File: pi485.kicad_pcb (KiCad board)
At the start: 2 copper layers, 48 x 70 mm, 28 parts, among them J1 RS485, P1 Rasperry Pi, P2 PWR, P3 Term, Q1 2N4401, Q2 2N4401, U1 NE555, U2 MAX485

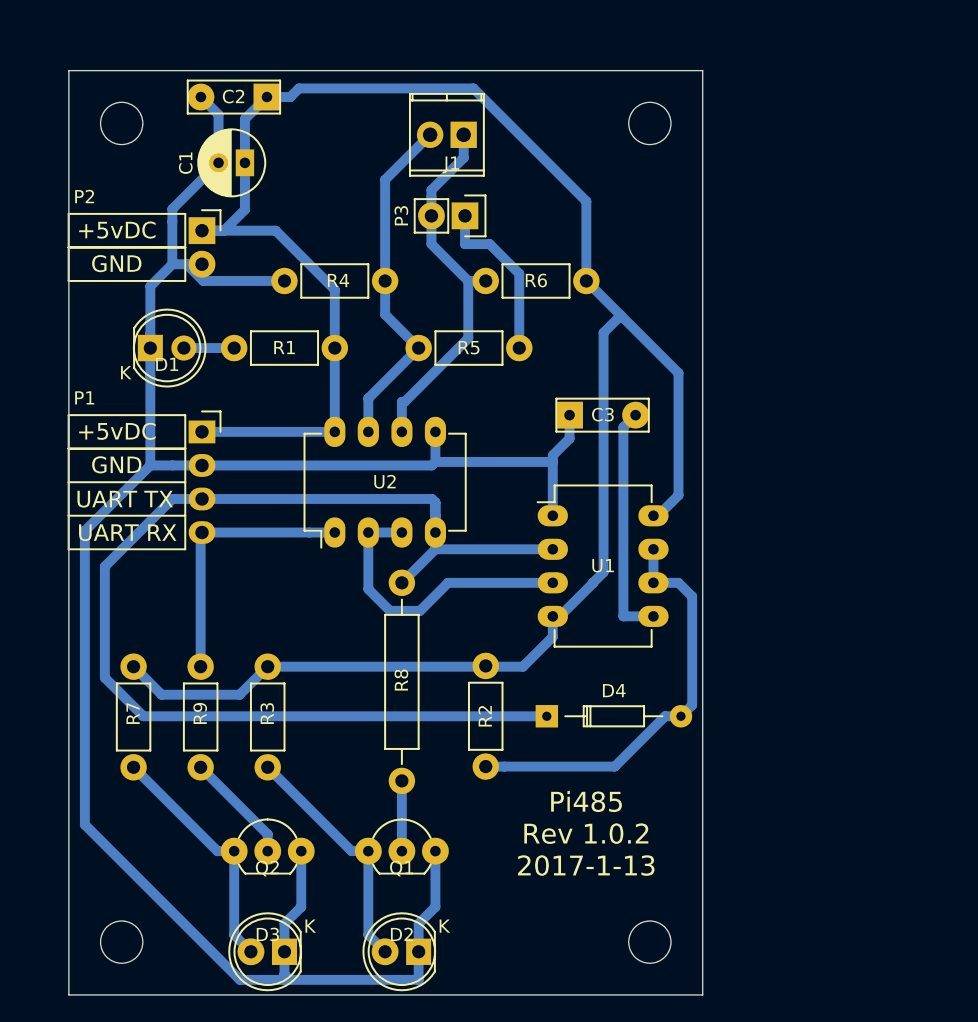
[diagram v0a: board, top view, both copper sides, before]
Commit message: * Rotated board 90 degrees. * Major update to footprints. Resistors are 10mm, LEDs are 3mm. * Manually re-routed / cleaned up traces & positiiong of quite a few things. * This could be pulled so much tighter, but to keep it 'simple soldering' I'm deliberately keeping big honkin traces with lots of clearance. * Fixed a major issue where I had accidentally forgotten the discharge capacitor by deleting the wrong one. The CTRL pin of the 555 should be jumperable to GND to keep the output of the 555 low, regardless of input (latch disable).
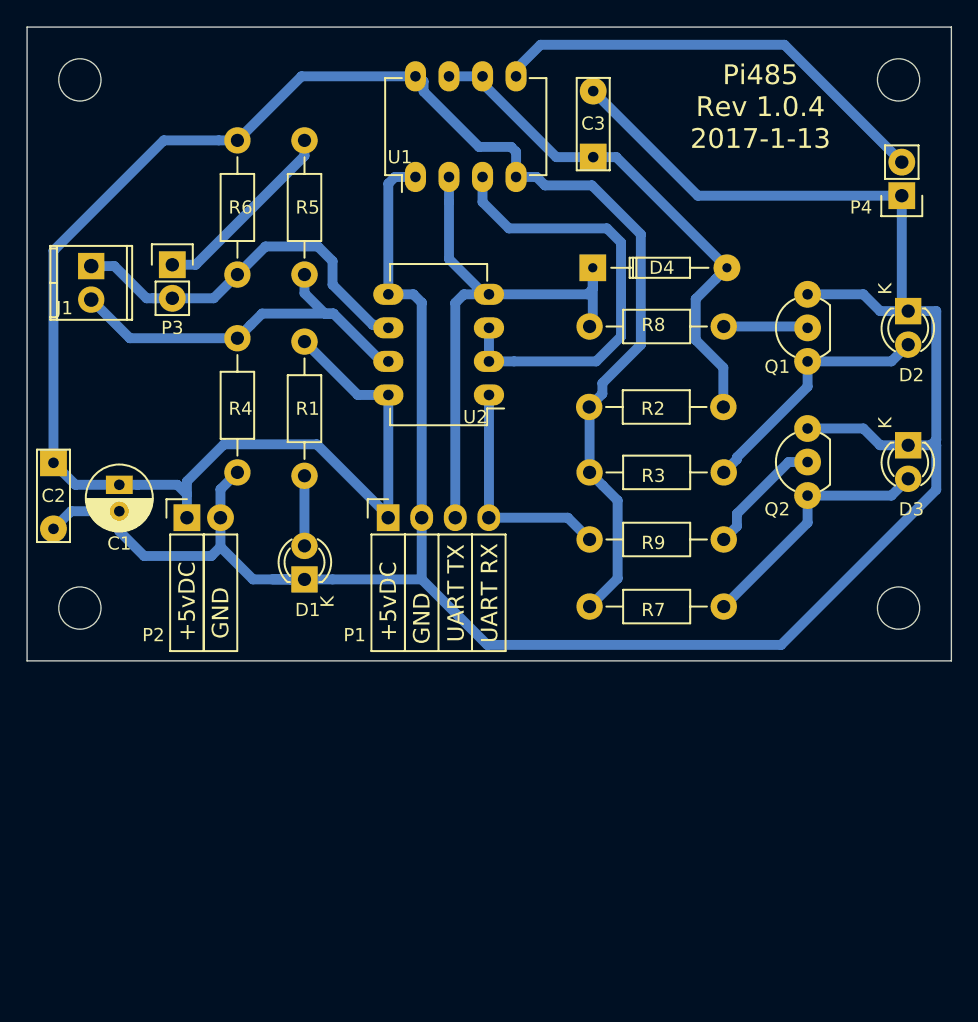
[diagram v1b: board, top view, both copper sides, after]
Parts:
- added P4: Latch Disable, Pin_Headers:Pin_Header_Straight_1x02, F.Cu at (78.6, 25.1)
- D1, D2, D3: footprint LEDs:LED-5MM -> LEDs:LED-3MM
- R1, R2, R3, R4, R5, R6, R7, R9: footprint Resistors_THT:Resistor_Horizontal_RM7mm -> Resistors_THT:Resistor_Horizontal_RM10mm
- R8: footprint Resistors_THT:Resistor_Horizontal_RM15mm -> Resistors_THT:Resistor_Horizontal_RM10mm
- moved REF03 68.0 mm to (78.3, 16.3), turned to 90 degrees
- moved REF04 64.0 mm to (78.3, 56.3), turned to 90 degrees
- moved D2 61.1 mm to (79.1, 33.8), turned to 270 degrees
- moved D3 60.8 mm to (79.1, 44.0), turned to 270 degrees
- moved Q2 51.1 mm to (71.4, 47.8), turned to 90 degrees
- moved Q1 49.8 mm to (71.4, 37.6), turned to 90 degrees
- moved R7 46.3 mm to (65.1, 56.2), turned to 180 degrees
- moved REF02 43.3 mm to (16.3, 16.3), turned to 90 degrees
- moved R9 43.2 mm to (65.1, 51.1), turned to 180 degrees
- moved R8 42.2 mm to (65.1, 35.0), turned to 180 degrees
- moved R3 41.1 mm to (65.1, 46.0), turned to 180 degrees
- moved REF01 36.8 mm to (16.3, 56.3), turned to 90 degrees
- moved D4 34.1 mm to (55.2, 30.5)
- moved R2 32.6 mm to (65.1, 41.1), turned to 180 degrees
- moved C2 32.1 mm to (14.3, 45.3), turned to 270 degrees
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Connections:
- C3 pad 1: GND -> Net-(C3-Pad1)
- C3 pad 2: Net-(C3-Pad2) -> GND
- D4 pad 2: Net-(D4-Pad2) -> Net-(C3-Pad1)
- R2 pad 1: Net-(D4-Pad2) -> Net-(C3-Pad1)
- U1 pad 5: Net-(C3-Pad2) -> Net-(P4-Pad2)
- U1 pad 6: Net-(D4-Pad2) -> Net-(C3-Pad1)
- U1 pad 7: Net-(D4-Pad2) -> Net-(C3-Pad1)
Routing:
- net /(TXDO)_GPIO14: track 88.7 -> 43.9 mm
- net Net-(C3-Pad1): track 0.00 -> 39.7 mm
- net Net-(P4-Pad2): track 0.00 -> 34.2 mm
- net Net-(D4-Pad2): track 31.1 -> 0.00 mm
- net GND: track 161.8 -> 192.4 mm
- net Net-(C3-Pad2): track 17.9 -> 0.00 mm
- net Net-(U1-Pad3): track 22.4 -> 35.2 mm
- net VCC: track 163.2 -> 154.5 mm
- net Net-(J1-Pad2): track 26.5 -> 30.2 mm
- net /(RXDO)_GPIO15: track 20.3 -> 17.6 mm
- net Net-(P3-Pad1): track 12.8 -> 14.6 mm
- net Net-(D1-Pad2): track 3.81 -> 5.56 mm
- net Net-(Q2-Pad2): track 8.45 -> 9.97 mm
- net Net-(Q1-Pad2): track 5.32 -> 6.39 mm
- net Net-(D2-Pad2): track 18.4 -> 19.2 mm
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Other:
- board size 48 x 70 mm -> 70 x 48 mm
- board text added: "Pi485 Rev 1.0.4 2017-1-13"
- board text removed: "Pi485 Rev 1.0.2 2017-1-13"

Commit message: Oh yeah, the date.
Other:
- board text added: "Pi485 Rev 1.0.4 2017-1-16"
- board text removed: "Pi485 Rev 1.0.4 2017-1-13"
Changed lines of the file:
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@@
     (effects (font (size 1.25 1.25) (thickness 0.2)))
   )
-  (gr_text "Pi485\nRev 1.0.4\n2017-1-13" (at 67.871 18.36) (layer F.SilkS)
+  (gr_text "Pi485\nRev 1.0.4\n2017-1-16" (at 67.871 18.36) (layer F.SilkS)
     (effects (font (size 1.5 1.5) (thickness 0.3)))
   )

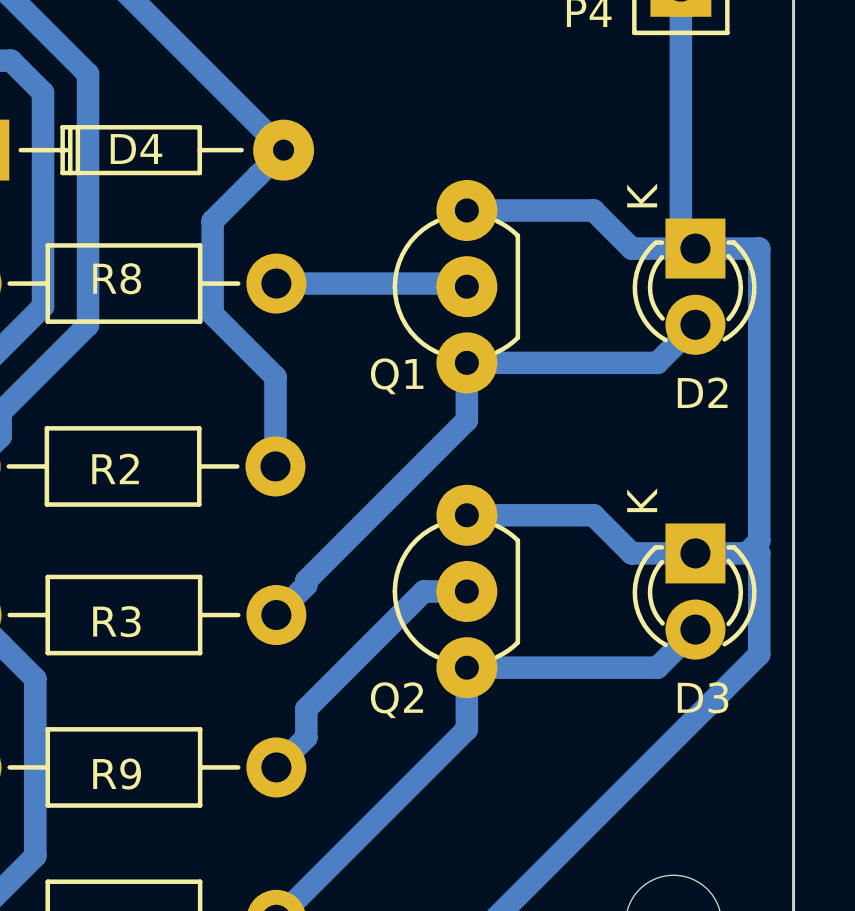
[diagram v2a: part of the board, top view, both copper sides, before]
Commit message: Fixed the footprint issues with the 2N4401 transistors being 'backwards'
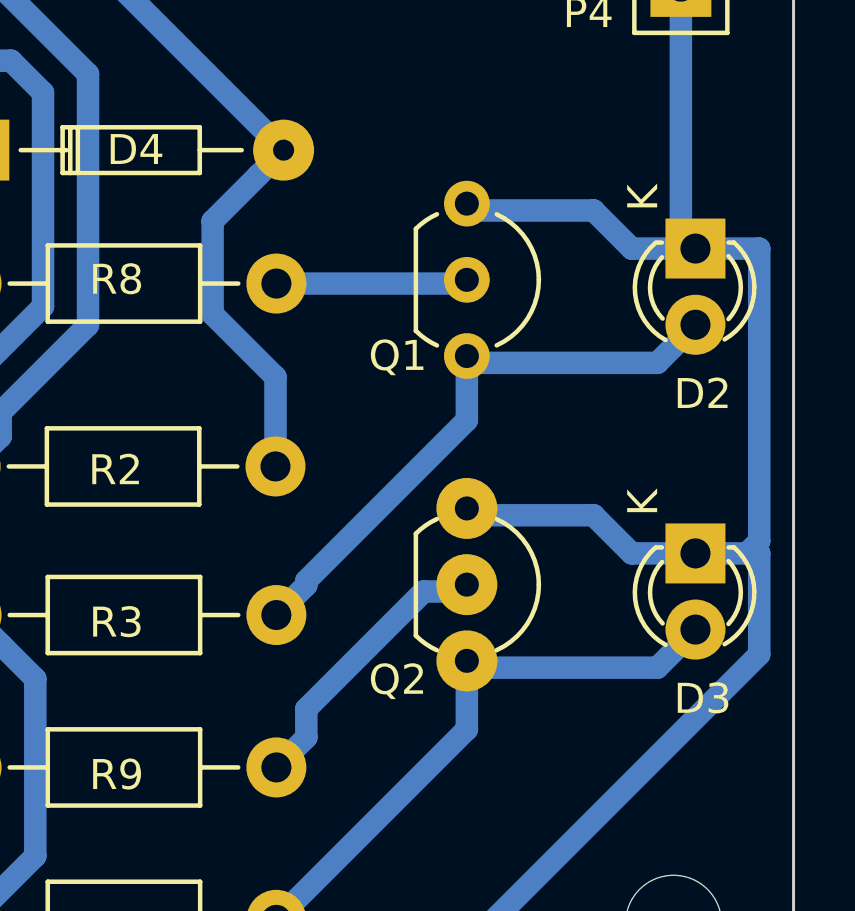
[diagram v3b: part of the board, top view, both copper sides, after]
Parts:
- moved Q1 5.31 mm to (71.4, 32.3), turned to 270 degrees
- moved Q2 5.31 mm to (71.4, 42.5), turned to 270 degrees
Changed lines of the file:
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@@
   (general
     (links 51)
-    (no_connects 0)
+    (no_connects 1)
     (area 10.622919 6.135856 84.172919 66.500142)
     (thickness 1.6)
@@
     (add_net VCC)
   )
+  (module TO_SOT_Packages_THT:TO-92_Inline_Wide placed (layer F.Cu)
+    (at 71.440419 42.49 270)
+    (descr "TO-92 leads in-line, wide, drill 0.8mm (see NXP sot054_po.pdf)")
+    (tags "to-92 sc-43 sc-43a sot54 PA33 transistor")
+    (fp_text reference Q2 (at 5.715 2.299419 360) (layer F.SilkS)
+      (effects (font (size 1 1) (thickness 0.15)))
+    )
+    (fp_text value 2N4401 (at -1.905 0.394419 360) (layer F.Fab)
+      (effects (font (size 1 1) (thickness 0.15)))
+    )
+    (fp_line (start 6.1 1.95) (end 6.1 -2.65) (layer F.CrtYd) (width 0.05))
+    (fp_line (start -1 -2.65) (end 6.1 -2.65) (layer F.CrtYd) (width 0.05))
+    (fp_arc (start 2.54 0) (end 2.54 -2.4) (angle 65.55604127) (layer F.SilkS) (width 0.15))
+    (fp_arc (start 2.54 0) (end 2.54 -2.4) (angle -65.55604127) (layer F.SilkS) (width 0.15))
+    (fp_line (start 0.84 1.7) (end 4.24 1.7) (layer F.SilkS) (width 0.15))
+    (fp_line (start -1 1.95) (end 6.1 1.95) (layer F.CrtYd) (width 0.05))
+    (fp_line (start -1 1.95) (end -1 -2.65) (layer F.CrtYd) (width 0.05))
+    (fp_arc (start 2.54 0) (end 4.24 1.7) (angle -20.5) (layer F.SilkS) (width 0.15))
+    (fp_arc (start 2.54 0) (end 0.84 1.7) (angle 20.5) (layer F.SilkS) (width 0.15))
+    (pad 1 thru_hole circle (at 5.08 0) (size 2.032 2.032) (drill 0.8) (layers *.Cu *.Mask)
+      (net 4 "Net-(D3-Pad2)"))
+    (pad 3 thru_hole circle (at 0 0) (size 2.032 2.032) (drill 0.8) (layers *.Cu *.Mask)
+      (net 2 GND))
+    (pad 2 thru_hole circle (at 2.54 0) (size 2.032 2.032) (drill 0.8) (layers *.Cu *.Mask)
+      (net 5 "Net-(Q2-Pad2)"))
+    (model TO_SOT_Packages_THT.3dshapes/TO-92_Inline_Wide.wrl
+      (at (xyz 0.1 0 0))
+      (scale (xyz 1 1 1))
+      (rotate (xyz 0 0 -90))
+    )
+  )
+  (module TO_SOT_Packages_THT:TO-92_Inline_Wide (layer F.Cu)
+    (at 71.440419 32.33 270)
+    (descr "TO-92 leads in-line, wide, drill 0.8mm (see NXP sot054_po.pdf)")
+    (tags "to-92 sc-43 sc-43a sot54 PA33 transistor")
+    (fp_text reference Q1 (at 5.08 2.299419 540) (layer F.SilkS)
+      (effects (font (size 1 1) (thickness 0.15)))
+    )
+    (fp_text value 2N4401 (at -1.905 0.394419 360) (layer F.Fab)
+      (effects (font (size 1 1) (thickness 0.15)))
+    )
+    (fp_line (start 6.1 1.95) (end 6.1 -2.65) (layer F.CrtYd) (width 0.05))
+    (fp_line (start -1 -2.65) (end 6.1 -2.65) (layer F.CrtYd) (width 0.05))
+    (fp_arc (start 2.54 0) (end 2.54 -2.4) (angle 65.55604127) (layer F.SilkS) (width 0.15))
+    (fp_arc (start 2.54 0) (end 2.54 -2.4) (angle -65.55604127) (layer F.SilkS) (width 0.15))
+    (fp_line (start 0.84 1.7) (end 4.24 1.7) (layer F.SilkS) (width 0.15))
+    (fp_line (start -1 1.95) (end 6.1 1.95) (layer F.CrtYd) (width 0.05))
+    (fp_line (start -1 1.95) (end -1 -2.65) (layer F.CrtYd) (width 0.05))
+    (fp_arc (start 2.54 0) (end 4.24 1.7) (angle -20.5) (layer F.SilkS) (width 0.15))
+    (fp_arc (start 2.54 0) (end 0.84 1.7) (angle 20.5) (layer F.SilkS) (width 0.15))
+    (pad 1 thru_hole circle (at 5.08 0) (size 1.524 1.524) (drill 0.8) (layers *.Cu *.Mask)
+      (net 3 "Net-(D2-Pad2)"))
+    (pad 3 thru_hole circle (at 0 0) (size 1.524 1.524) (drill 0.8) (layers *.Cu *.Mask)
+      (net 2 GND))
+    (pad 2 thru_hole circle (at 2.54 0) (size 1.524 1.524) (drill 0.8) (layers *.Cu *.Mask)
+      (net 1 "Net-(Q1-Pad2)"))
+    (model TO_SOT_Packages_THT.3dshapes/TO-92_Inline_Wide.wrl
+      (at (xyz 0.1 0 0))
+      (scale (xyz 1 1 1))
+      (rotate (xyz 0 0 -90))
+    )
+  )
   (module Resistors_THT:Resistor_Horizontal_RM10mm (layer F.Cu)
     (at 65.090419 34.994199 180)
@@
     )
   )
-  (module TO_SOT_Packages_THT:TO-92_Inline_Wide placed (layer F.Cu)
-    (at 71.440419 47.797999 90)
-    (descr "TO-92 leads in-line, wide, drill 0.8mm (see NXP sot054_po.pdf)")
-    (tags "to-92 sc-43 sc-43a sot54 PA33 transistor")
-    (fp_text reference Q2 (at -1.042001 -2.299419 180) (layer F.SilkS)
-      (effects (font (size 1 1) (thickness 0.15)))
-    )
-    (fp_text value 2N4401 (at 7.212999 -0.394419 180) (layer F.Fab)
-      (effects (font (size 1 1) (thickness 0.15)))
-    )
-    (fp_line (start 6.1 1.95) (end 6.1 -2.65) (layer F.CrtYd) (width 0.05))
-    (fp_line (start -1 -2.65) (end 6.1 -2.65) (layer F.CrtYd) (width 0.05))
-    (fp_arc (start 2.54 0) (end 2.54 -2.4) (angle 65.55604127) (layer F.SilkS) (width 0.15))
-    (fp_arc (start 2.54 0) (end 2.54 -2.4) (angle -65.55604127) (layer F.SilkS) (width 0.15))
-    (fp_line (start 0.84 1.7) (end 4.24 1.7) (layer F.SilkS) (width 0.15))
-    (fp_line (start -1 1.95) (end 6.1 1.95) (layer F.CrtYd) (width 0.05))
-    (fp_line (start -1 1.95) (end -1 -2.65) (layer F.CrtYd) (width 0.05))
-    (fp_arc (start 2.54 0) (end 4.24 1.7) (angle -20.5) (layer F.SilkS) (width 0.15))
-    (fp_arc (start 2.54 0) (end 0.84 1.7) (angle 20.5) (layer F.SilkS) (width 0.15))
-    (pad 1 thru_hole circle (at 0 0 180) (size 2.032 2.032) (drill 0.8) (layers *.Cu *.Mask)
-      (net 4 "Net-(D3-Pad2)"))
-    (pad 3 thru_hole circle (at 5.08 0 180) (size 2.032 2.032) (drill 0.8) (layers *.Cu *.Mask)
-      (net 2 GND))
-    (pad 2 thru_hole circle (at 2.54 0 180) (size 2.032 2.032) (drill 0.8) (layers *.Cu *.Mask)
-      (net 5 "Net-(Q2-Pad2)"))
-    (model TO_SOT_Packages_THT.3dshapes/TO-92_Inline_Wide.wrl
-      (at (xyz 0.1 0 0))
-      (scale (xyz 1 1 1))
-      (rotate (xyz 0 0 -90))
-    )
-  )
-  (module TO_SOT_Packages_THT:TO-92_Inline_Wide placed (layer F.Cu)
-    (at 71.440419 37.637999 90)
-    (descr "TO-92 leads in-line, wide, drill 0.8mm (see NXP sot054_po.pdf)")
-    (tags "to-92 sc-43 sc-43a sot54 PA33 transistor")
-    (fp_text reference Q1 (at -0.407001 -2.299419) (layer F.SilkS)
-      (effects (font (size 1 1) (thickness 0.15)))
-    )
-    (fp_text value 2N4401 (at 7.212999 -0.394419 180) (layer F.Fab)
-      (effects (font (size 1 1) (thickness 0.15)))
-    )
-    (fp_arc (start 2.54 0) (end 0.84 1.7) (angle 20.5) (layer F.SilkS) (width 0.15))
-    (fp_arc (start 2.54 0) (end 4.24 1.7) (angle -20.5) (layer F.SilkS) (width 0.15))
-    (fp_line (start -1 1.95) (end -1 -2.65) (layer F.CrtYd) (width 0.05))
-    (fp_line (start -1 1.95) (end 6.1 1.95) (layer F.CrtYd) (width 0.05))
-    (fp_line (start 0.84 1.7) (end 4.24 1.7) (layer F.SilkS) (width 0.15))
-    (fp_arc (start 2.54 0) (end 2.54 -2.4) (angle -65.55604127) (layer F.SilkS) (width 0.15))
-    (fp_arc (start 2.54 0) (end 2.54 -2.4) (angle 65.55604127) (layer F.SilkS) (width 0.15))
-    (fp_line (start -1 -2.65) (end 6.1 -2.65) (layer F.CrtYd) (width 0.05))
-    (fp_line (start 6.1 1.95) (end 6.1 -2.65) (layer F.CrtYd) (width 0.05))
-    (pad 2 thru_hole circle (at 2.54 0 180) (size 2.032 2.032) (drill 0.8) (layers *.Cu *.Mask)
-      (net 1 "Net-(Q1-Pad2)"))
-    (pad 3 thru_hole circle (at 5.08 0 180) (size 2.032 2.032) (drill 0.8) (layers *.Cu *.Mask)
-      (net 2 GND))
-    (pad 1 thru_hole circle (at 0 0 180) (size 2.032 2.032) (drill 0.8) (layers *.Cu *.Mask)
-      (net 3 "Net-(D2-Pad2)"))
-    (model TO_SOT_Packages_THT.3dshapes/TO-92_Inline_Wide.wrl
-      (at (xyz 0.1 0 0))
-      (scale (xyz 1 1 1))
-      (rotate (xyz 0 0 -90))
-    )
-  )
